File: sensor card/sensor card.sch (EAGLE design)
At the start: 37 parts, among them J1 MJ-3536N, J2 MJ-3536N, U1 PCA9306, X1 S4B-XH-A, X2 S4B-XH-A

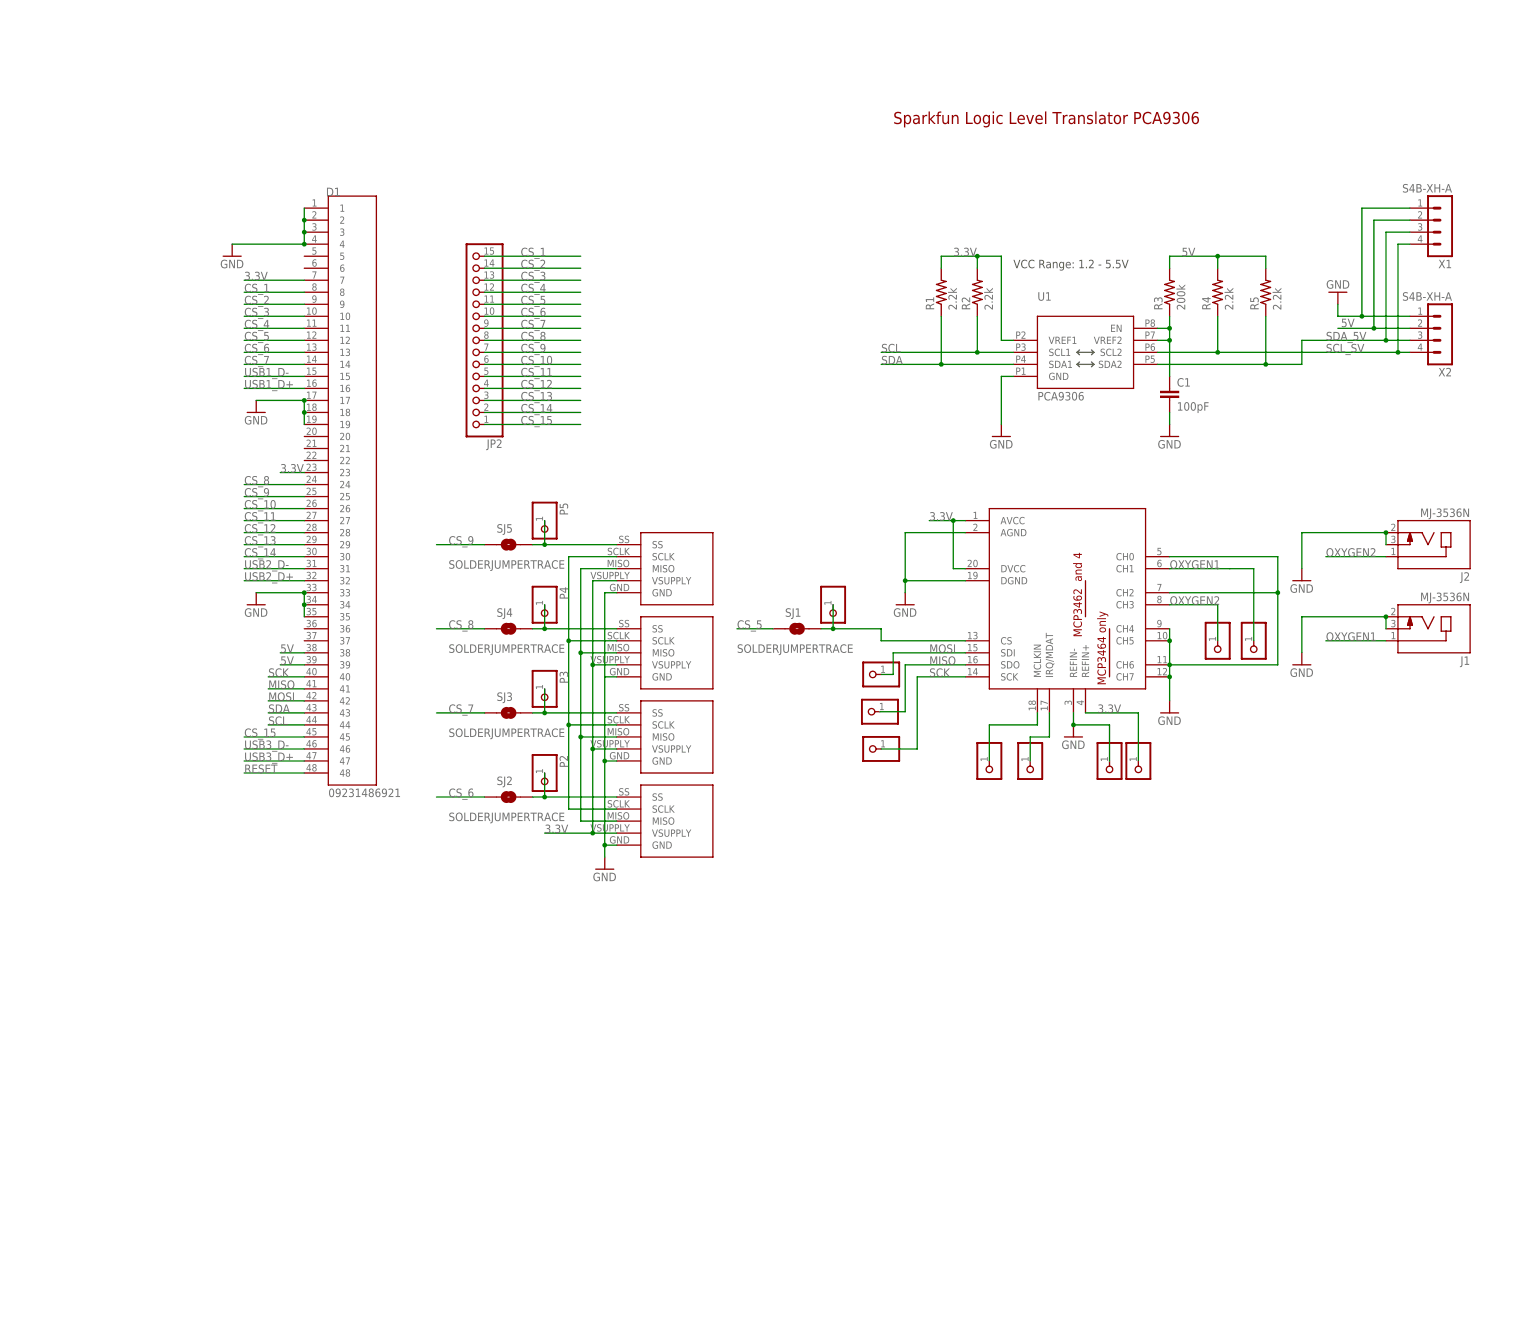
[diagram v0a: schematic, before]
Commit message: added the new oxygen sensing system to the control module
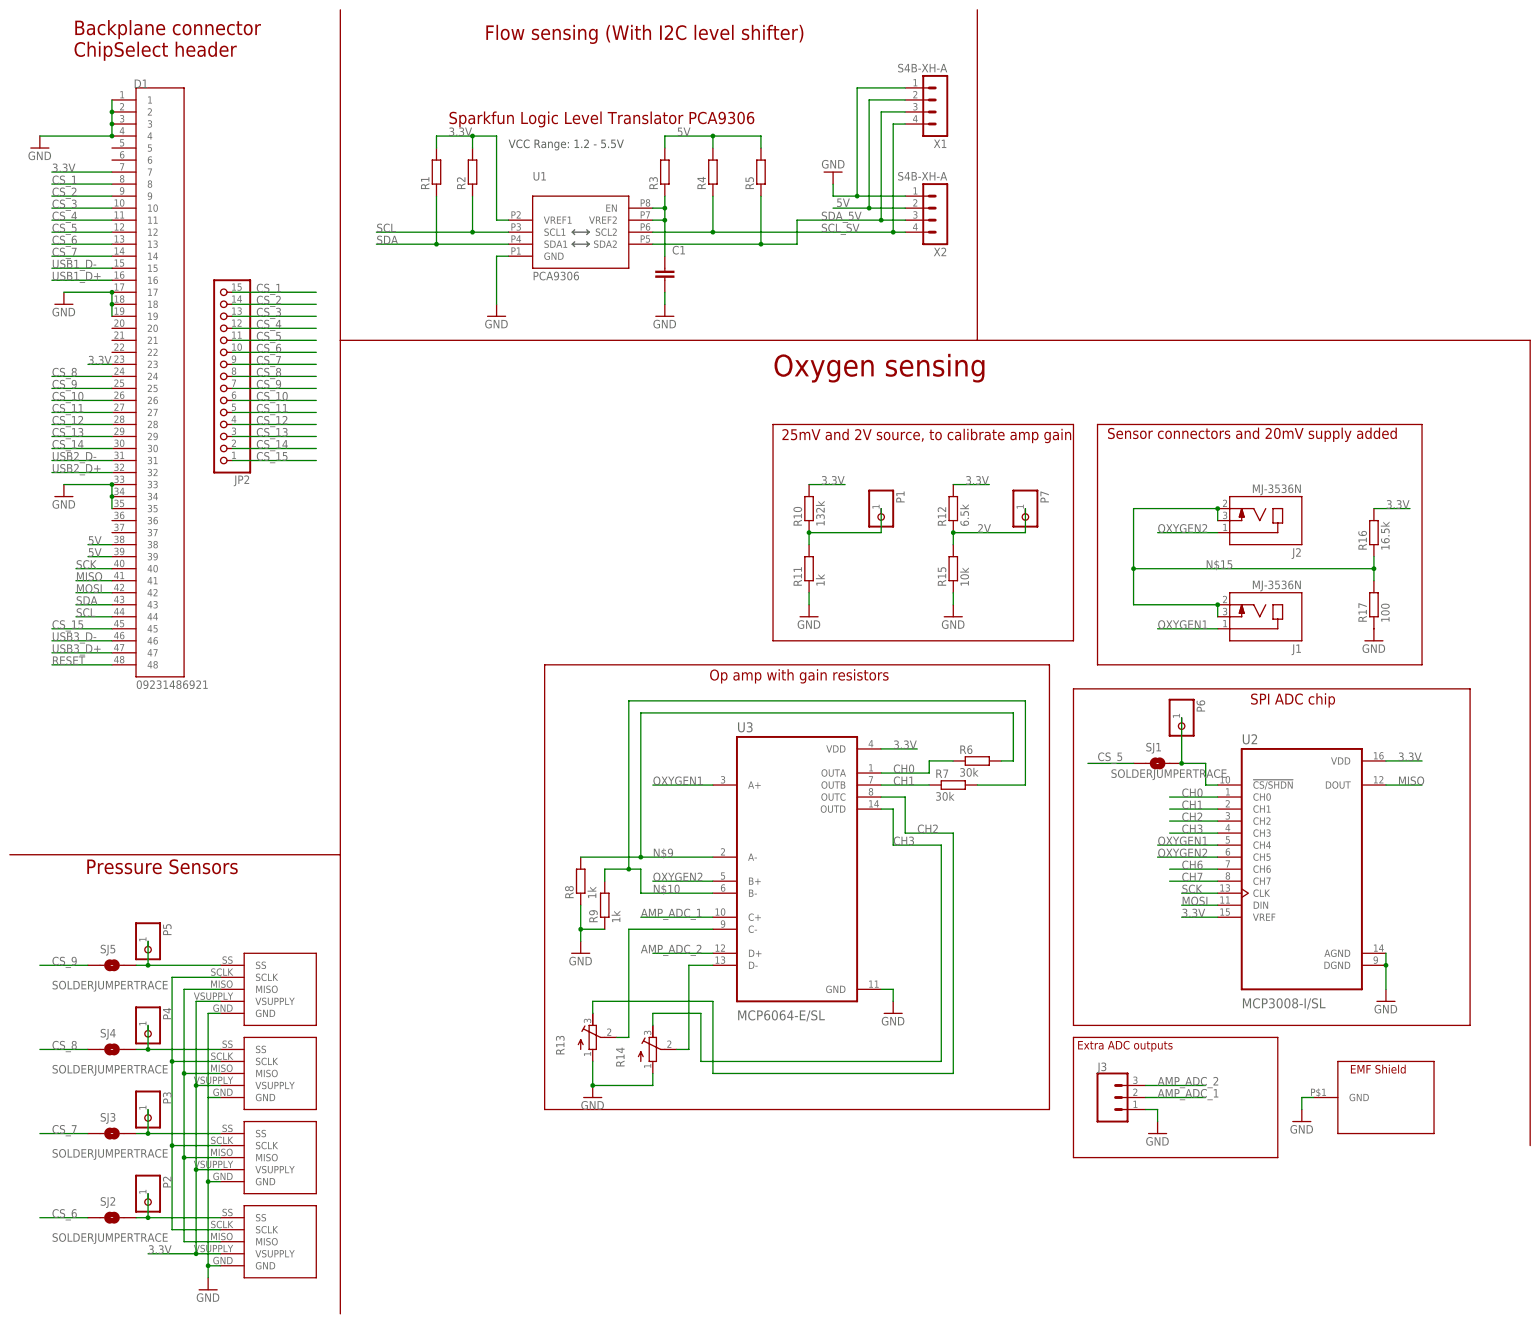
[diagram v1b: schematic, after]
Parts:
- removed JP1, JP10, JP3, JP4, JP5, JP6, JP7, JP8, JP9: (no value), pinhead:PINHD-1X1
- added J3: (no value), SparkFun-Connectors:CONN_03
- added P6, P7: (no value), pinhead:PINHD-1X1
- added R10: 132k, eagle-ltspice:R
- added R11, R8, R9: 1k, eagle-ltspice:R
- added R12: 6.5k, eagle-ltspice:R
- added R13, R14: (no value), rcl:R-TRIMM3214W
- added R15: 10k, eagle-ltspice:R
- added R16: 16.5k, eagle-ltspice:R
- added R17: 100, eagle-ltspice:R
- added R6, R7: 30k, eagle-ltspice:R
- added U2: MCP3008-I/SL, MCP3008-I_SL:MCP3008-I/SL
- added U3: MCP6064-E/SL, MCP6064-E_SL:MCP6064-E/SL
- C1: device SparkFun-Capacitors:100PF-0603-50V-5% -> rcl:C-EUC0805
- R1, R2, R4, R5: device SparkFun-Resistors:2.2KOHM-0603-1/10W-1% -> eagle-ltspice:R
- R3: value 200k -> 200K; device SparkFun-Resistors:200KOHM-0603-1/10W-1% -> eagle-ltspice:R
- U$2: value MCP346X-E/ST -> EMI_SHIELD; device MCP346XRT-E:ST:MCP346X-E/ST -> emi cap:EMI_SHIELD
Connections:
- removed net IRQ/MDAT: JP3.1, U$2.IRQ/MDAT
- removed net MCLKIN: JP1.1, U$2.MCLKIN
- new net 2V: P7.1, R12.1, R15.2
- new net 50MILIVOLT: P1.1, R10.1, R11.2
- new net AMP_ADC_1: J3.2, U3.C+
- new net AMP_ADC_2: J3.3, U3.D+
- new net CH0: R6.1, U2.CH0, U3.OUTA
- new net CH1: R7.1, U2.CH1, U3.OUTB
- new net CH2: R13.E, U2.CH2, U3.OUTC
- new net CH3: R14.E, U2.CH3, U3.OUTD
- new net CH6: U2.CH6
- new net CH7: U2.CH7
- new net N$10: R7.2, R9.2, U3.B-
- new net N$15: J1.2, J1.3, J2.2, J2.3, R16.1, R17.2
- new net N$2: R14.S, U3.D-
- new net N$8: R13.S, U3.C-
- new net N$9: R6.2, R8.2, U3.A-
- net 3.3V: now also R10.2, R12.2, R16.2, U2.VDD, U2.VREF, U3.VDD; no longer JP9.1, U$2.AVCC, U$2.DVCC, U$2.REFIN+
- net GND: now also J3.1, R11.1, R13.A, R14.A, R15.1, R17.1, R8.1, R9.1, U$2.GND, U2.AGND, U2.DGND, U3.GND; no longer J1.2, J1.3, J2.2, J2.3, JP10.1, U$2.AGND, U$2.CH0, U$2.CH2, U$2.CH4, U$2.CH5, U$2.CH6, U$2.CH7, U$2.DGND, U$2.REFIN-
- net MISO: now also U2.DOUT; no longer JP5.1, U$2.SDO
- net MOSI: now also U2.DIN; no longer JP6.1, U$2.SDI
- net N$3: now also P6.1, U2.!CS/SHDN; no longer P1.1, U$2.CS
- net OXYGEN1: now also U2.CH4, U3.A+; no longer JP8.1, U$2.CH1
- net OXYGEN2: now also U2.CH5, U3.B+; no longer JP7.1, U$2.CH3
- net SCK: now also U2.CLK; no longer JP4.1, U$2.SCK
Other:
- note added: "25mV and 2V source, to calibrate amp gain"
- note added: "Backplane connector ChipSelect header"
- note added: "Extra ADC outputs"
- note added: "Flow sensing (With I2C level shifter)"
- note added: "Op amp with gain resistors"
- note added: "Oxygen sensing"
- note added: "Pressure Sensors"
- note added: "SPI ADC chip"
- note added: "Sensor connectors and 20mV supply added"
- moved on the sheet: C1, D1, J1, J2, JP2, P2, P3, P4, P5, SJ1, SJ2, SJ3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

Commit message: updated libraries to generate better bom's
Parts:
- C1: device rcl:C-EUC0805 -> SparkFun-Passives:CAP0805
- R1, R2, R3, R4, R5: device eagle-ltspice:R -> SparkFun-Passives:RESISTOR0805-RES
- R10: value 132k -> 132k, 1%; device eagle-ltspice:R -> SparkFun-Passives:RESISTOR0805-RES
- R11: value 1k -> 1k, 1%; device eagle-ltspice:R -> SparkFun-Passives:RESISTOR0805-RES
- R12: value 6.5k -> 6.5k, 1%; device eagle-ltspice:R -> SparkFun-Passives:RESISTOR0805-RES
- R15: value 10k -> 10k, 1%; device eagle-ltspice:R -> SparkFun-Passives:RESISTOR0805-RES
- R16: value 16.5k -> 16.5k, 1%; device eagle-ltspice:R -> SparkFun-Passives:RESISTOR0805-RES
- R17: value 100 -> 100, 1%; device eagle-ltspice:R -> SparkFun-Passives:RESISTOR0805-RES
- R6, R7: value 30k -> 30k, 0.1%, 25ppm/C; device eagle-ltspice:R -> SparkFun-Passives:RESISTOR0805-RES
- R8, R9: value 1k -> 1k, 0.1%, 25ppm/C; device eagle-ltspice:R -> SparkFun-Passives:RESISTOR0805-RES
- U1: MANUFACTURER-PART-NUMBER (none) -> PCA9306D,118
